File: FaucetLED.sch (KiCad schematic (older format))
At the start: 34 parts, among them P1 CONN_01X03, P2 CONN_01X02, P3 CONN_01X02, P4 CONN_01X03, Q1 BSS138, Q2 BSS138, Q3 BSS138, U1 TLV70033DDC, U2 STM32L052KxTx, U3 NCV551SN50T1G

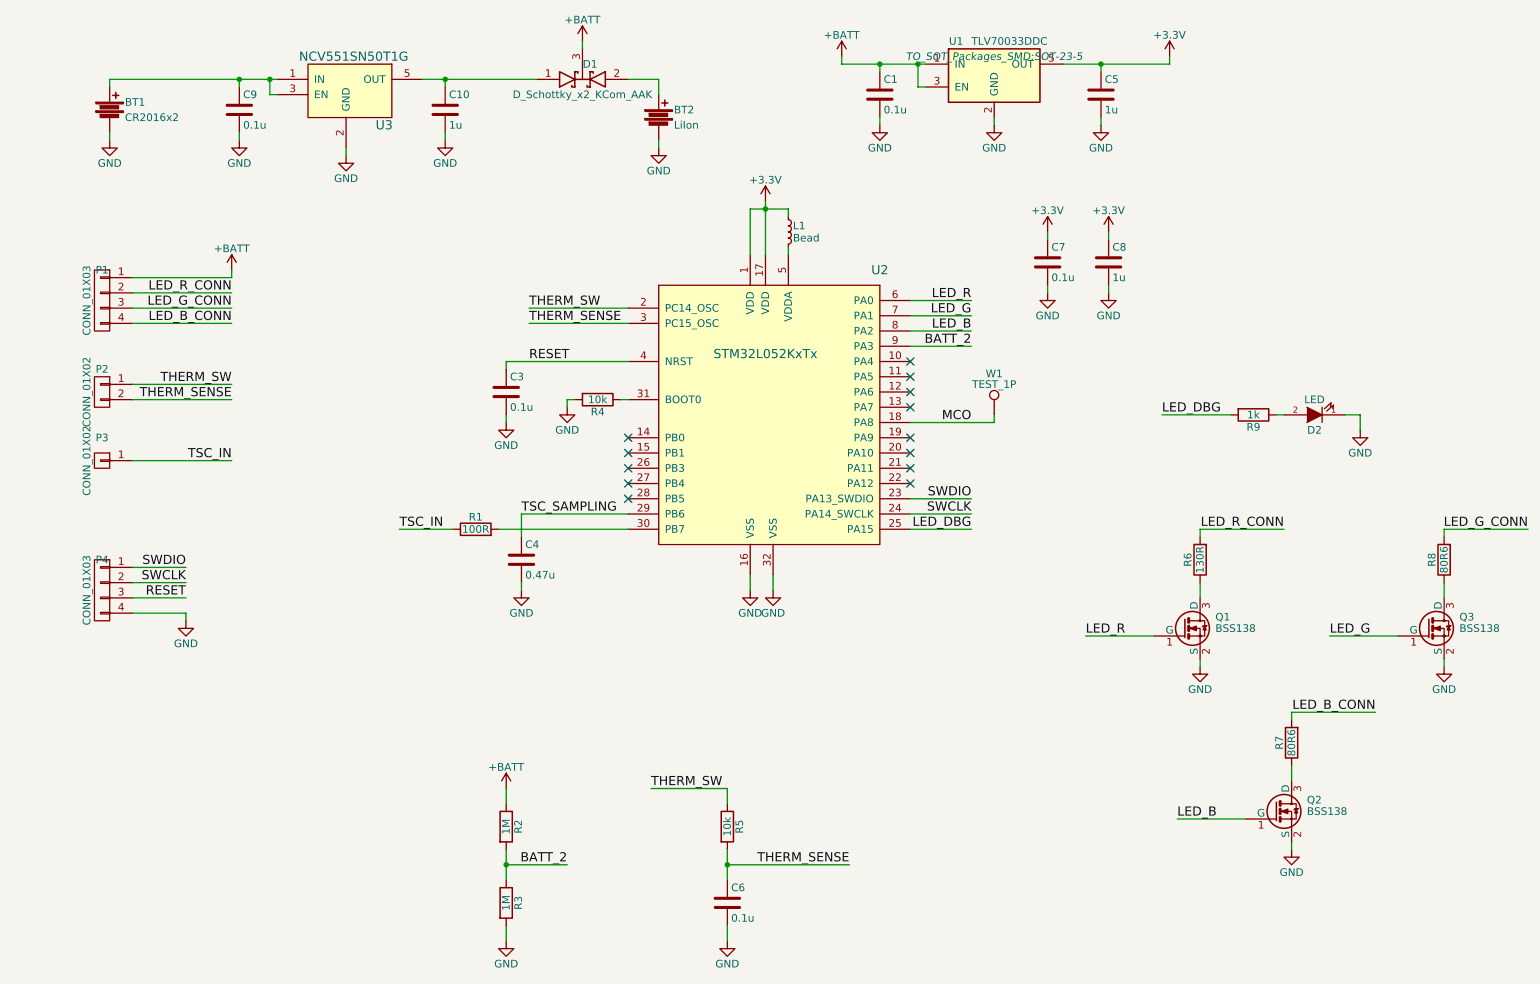
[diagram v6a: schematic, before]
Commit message: First pass of PCB layout complete. Fixed a couple incorrect ADC pins.
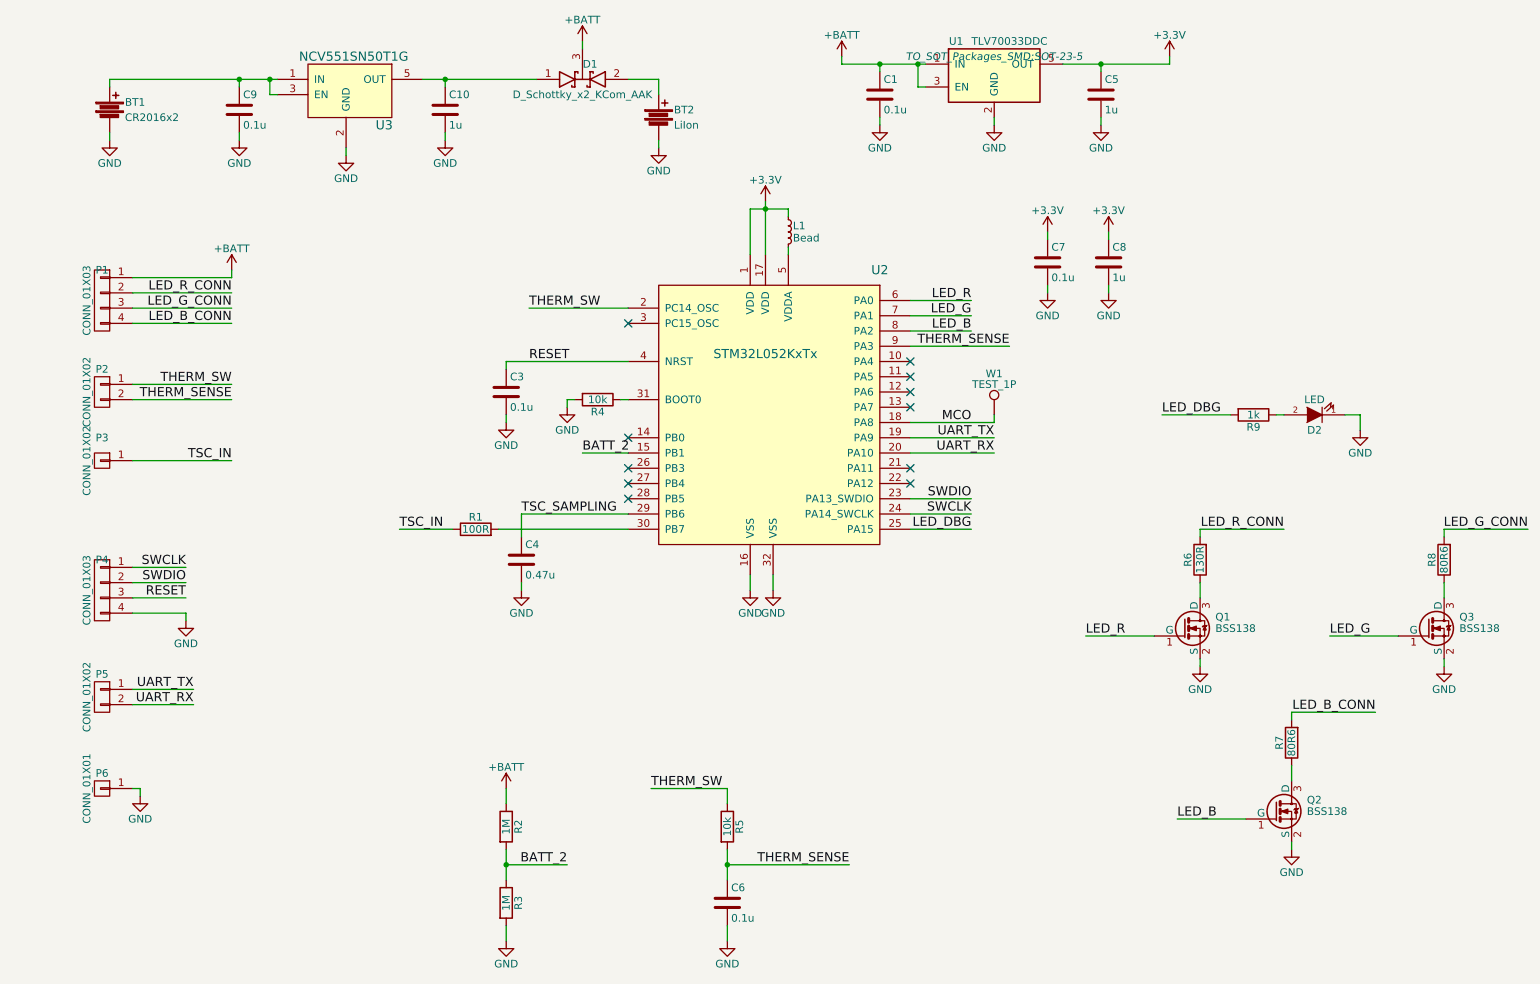
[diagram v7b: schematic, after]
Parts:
- added P5: CONN_01X02, Pin_Headers:Pin_Header_Straight_1x02_Pitch2.54mm, symbol CONN_01X02
- added P6: CONN_01X01, Pin_Headers:Pin_Header_Straight_1x01_Pitch2.54mm, symbol CONN_01X01
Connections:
- net BATT_2: now also U2.15 (PB1); no longer U2.9 (PA3)
- net GND: now also P6.1 (P1)
- net SWCLK: now also P4.1 (P1); no longer P4.2 (P2)
- net SWDIO: now also P4.2 (P2); no longer P4.1 (P1)
- net THERM_SENSE: now also U2.9 (PA3); no longer U2.3 (PC15_OSC)
- net UART_TX: now reaches U2.19 (PA9)
- net UART_TX: now also P5.1 (P1)
- net UART_RX: now reaches U2.20 (PA10)
- net UART_RX: now also P5.2 (P2)
- no-connect marks 13 -> 11
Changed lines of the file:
@@
-	1    0    0    -1
-$EndComp
-$Comp
-L STM32L052KxTx U2
-U 1 1 58AA48CE
-P 5600 3100
-F 0 "U2" H 6400 3900 60  0000 C CNN
-F 1 "STM32L052KxTx" H 5650 3350 60  0000 C CNN
-F 2 "Housings_QFP:LQFP-32_7x7mm_Pitch0.8mm" H 5500 2250 60  0001 C CNN
-F 3 "" H 5500 2250 60  0001 C CNN
-F 4 "497-14904-ND" H 5600 3100 60  0001 C CNN "DigiKey PN"
-F 5 "STM32L052K8T6" H 5600 3100 60  0001 C CNN "Manufacturer PN"
-	1    5600 3100
 	1    0    0    -1
 $EndComp
@@
 Text Label 4100 2550 0    60   ~ 0
 THERM_SW
-Text Label 4100 2650 0    60   ~ 0
+Text Label 7250 2800 2    60   ~ 0
 THERM_SENSE
 $Comp
@@
 Wire Wire Line
 	4100 2550 4750 2550
-Wire Wire Line
-	4100 2650 4750 2650
 Wire Wire Line
 	5700 4300 5700 4400
@@
 	-1   0    0    -1
 $EndComp
+Text Label 1850 4350 2    60   ~ 0
+SWDIO
 Text Label 1850 4250 2    60   ~ 0
-SWDIO
-Text Label 1850 4350 2    60   ~ 0
 SWCLK
 Text Label 1850 4450 2    60   ~ 0
@@
 	5400 6100 5400 6300
 NoConn ~ 4750 3400
-NoConn ~ 4750 3500
 NoConn ~ 4750 3600
 NoConn ~ 4750 3700
@@
 NoConn ~ 6600 3100
 NoConn ~ 6600 3200
-NoConn ~ 6600 3400
-NoConn ~ 6600 3500
 NoConn ~ 6600 3600
 NoConn ~ 6600 3700
@@
 Wire Wire Line
 	4350 6200 3950 6200
-Text Label 7000 2800 2    60   ~ 0
+Text Label 4450 3500 0    60   ~ 0
 BATT_2
-Wire Wire Line
-	7000 2800 6600 2800
 $Comp
 L D_Schottky_x2_KCom_AAK D1
@@
 Wire Wire Line
 	6400 950  6400 1000
+Wire Wire Line
+	4450 3500 4750 3500
+Wire Wire Line
+	7250 2800 6600 2800
+NoConn ~ 4750 2650
+$Comp
+L STM32L052KxTx U2
+U 1 1 58AA48CE
+P 5600 3100
+F 0 "U2" H 6400 3900 60  0000 C CNN
+F 1 "STM32L052KxTx" H 5650 3350 60  0000 C CNN
+F 2 "Housings_QFP:LQFP-32_7x7mm_Pitch0.8mm" H 5500 2250 60  0001 C CNN
+F 3 "" H 5500 2250 60  0001 C CNN
+F 4 "497-14904-ND" H 5600 3100 60  0001 C CNN "DigiKey PN"
+F 5 "STM32L052K8T6" H 5600 3100 60  0001 C CNN "Manufacturer PN"
+	1    5600 3100
+	1    0    0    -1
+$EndComp
+Text Label 7150 3400 2    60   ~ 0
+UART_TX
+Text Label 7150 3500 2    60   ~ 0
+UART_RX
+Wire Wire Line
+	7150 3400 6600 3400
+Wire Wire Line
+	6600 3500 7150 3500
+$Comp
+L CONN_01X02 P5
+U 1 1 58AE72EE
+P 1300 5100
+F 0 "P5" H 1300 5250 50  0000 C CNN
+F 1 "CONN_01X02" V 1400 5100 50  0000 C CNN
+F 2 "Pin_Headers:Pin_Header_Straight_1x02_Pitch2.54mm" H 1300 5100 50  0001 C CNN
+F 3 "" H 1300 5100 50  0000 C CNN
+	1    1300 5100
+	-1   0    0    -1
+$EndComp
+Text Label 1900 5050 2    60   ~ 0
+UART_TX
+Text Label 1900 5150 2    60   ~ 0
+UART_RX
+Wire Wire Line
+	1900 5150 1500 5150
+Wire Wire Line
+	1500 5050 1900 5050
+$Comp
+L CONN_01X01 P6
+U 1 1 58AE7B4F
+P 1300 5700
+F 0 "P6" H 1300 5800 50  0000 C CNN
+F 1 "CONN_01X01" V 1400 5700 50  0000 C CNN
+F 2 "Pin_Headers:Pin_Header_Straight_1x01_Pitch2.54mm" H 1300 5700 50  0001 C CNN
+F 3 "" H 1300 5700 50  0000 C CNN
+	1    1300 5700
+	-1   0    0    -1
+$EndComp
+$Comp
+L GND #PWR031
+U 1 1 58AE7D5E
+P 1550 5750
+F 0 "#PWR031" H 1550 5500 50  0001 C CNN
+F 1 "GND" H 1550 5600 50  0000 C CNN
+F 2 "" H 1550 5750 50  0000 C CNN
+F 3 "" H 1550 5750 50  0000 C CNN
+	1    1550 5750
+	1    0    0    -1
+$EndComp
+Wire Wire Line
+	1550 5750 1550 5700
+Wire Wire Line
+	1550 5700 1500 5700
 $EndSCHEMATC

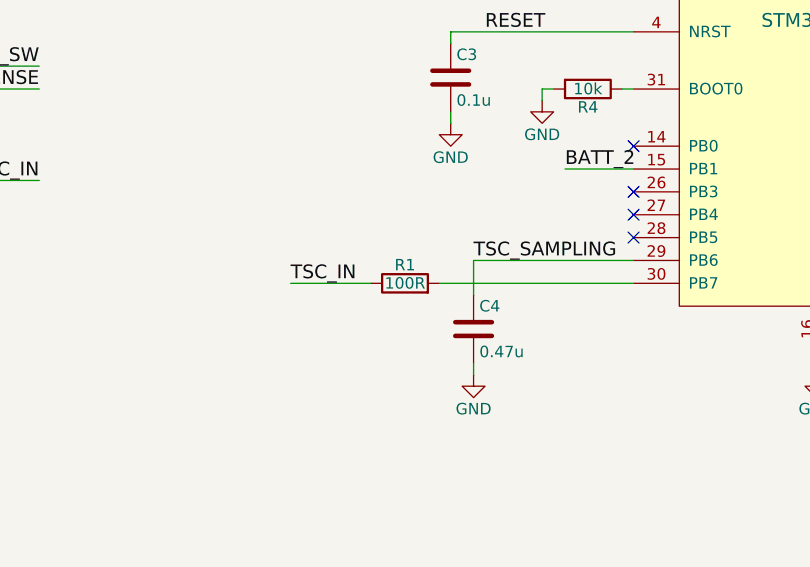
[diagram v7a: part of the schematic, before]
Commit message: Change TSC resistor to 130R for commonality. Update BOM.
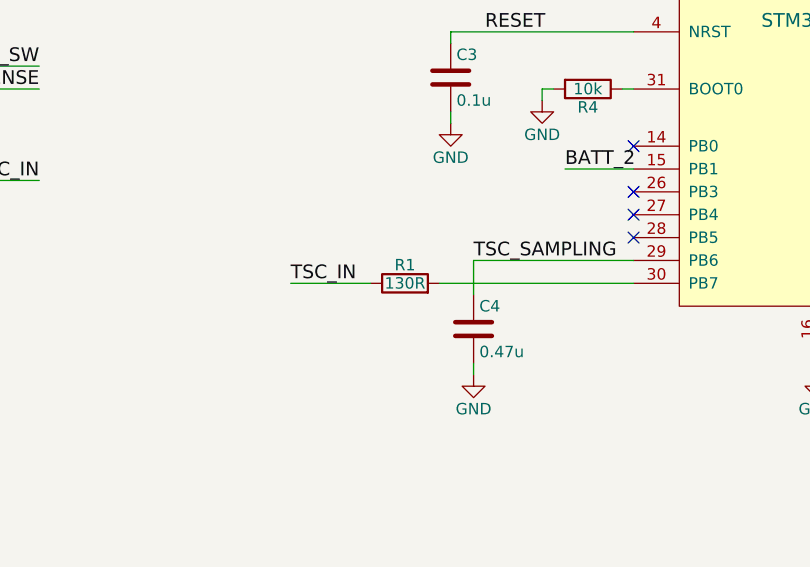
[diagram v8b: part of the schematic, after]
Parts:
- R1: value 100R -> 130R; DigiKey PN (none) -> 311-130HRCT-ND
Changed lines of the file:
@@
 P 3750 4000
 F 0 "R1" V 3830 4000 50  0000 C CNN
-F 1 "100R" V 3750 4000 50  0000 C CNN
+F 1 "130R" V 3750 4000 50  0000 C CNN
 F 2 "components:R_0603_0805" V 3680 4000 50  0001 C CNN
 F 3 "" H 3750 4000 50  0000 C CNN
+F 4 "311-130HRCT-ND" H 3750 4000 60  0001 C CNN "DigiKey PN"
 	1    3750 4000
 	0    -1   -1   0
